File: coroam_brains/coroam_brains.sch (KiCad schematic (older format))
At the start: 19 parts, among them U1 L7805, U2 mini_esp32

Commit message: trying schematic on new pc
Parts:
- C1, C2, C3, C4, C5: symbol Device:CP -> coroam_brains-rescue:CP-Device
- D1, D2: symbol Device:LED -> coroam_brains-rescue:LED-Device
- LCD_I2C1: symbol Connector:Screw_Terminal_01x04 -> coroam_brains-rescue:Screw_Terminal_01x04-Connector
- R1, R2, oneWirePup1: symbol Device:R -> coroam_brains-rescue:R-Device
- TempBreadBoard1, TempCasing1, TempElectronics1, TempLaser1, TempWater1: symbol Connector:Screw_Terminal_01x03 -> coroam_brains-rescue:Screw_Terminal_01x03-Connector
- U1: symbol Regulator_Linear:L7805 -> coroam_brains-rescue:L7805-Regulator_Linear
- U2: symbol laserhannes_custom:mini_esp32 -> coroam_brains-rescue:mini_esp32-laserhannes_custom
- lls1: symbol laserhannes_custom:level_shifter -> coroam_brains-rescue:level_shifter-laserhannes_custom
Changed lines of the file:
@@
 EESchema Schematic File Version 4
-LIBS:coroam_brains-cache
 EELAYER 30 0
 EELAYER END
@@
 $EndDescr
 $Comp
-L power:+3.3V #PWR018
+L coroam_brains-rescue:+3.3V-power #PWR018
 U 1 1 5F539EF8
 P 6550 2900
@@
 $EndComp
 $Comp
-L power:GND #PWR017
+L coroam_brains-rescue:GND-power #PWR017
 U 1 1 5F53B2BB
 P 6450 3500
@@
 Connection ~ 6450 3400
 $Comp
-L power:+5V #PWR015
+L coroam_brains-rescue:+5V-power #PWR015
 U 1 1 5F543A46
 P 6300 2900
@@
 	6300 3000 6250 3000
 $Comp
-L power:+5V #PWR02
+L coroam_brains-rescue:+5V-power #PWR02
 U 1 1 5F540B62
 P 1200 900
@@
 $EndComp
 $Comp
-L power:GND #PWR05
+L coroam_brains-rescue:GND-power #PWR05
 U 1 1 5F540B68
 P 1800 1750
@@
 $EndComp
 $Comp
-L Regulator_Linear:L7805 U1
+L coroam_brains-rescue:L7805-Regulator_Linear U1
 U 1 1 5F540B6E
 P 3250 950
@@
 $EndComp
 $Comp
-L power:+12V #PWR09
+L coroam_brains-rescue:+12V-power #PWR09
 U 1 1 5F540B74
 P 2750 900
@@
 	2750 950  2950 950
 $Comp
-L power:GND #PWR010
+L coroam_brains-rescue:GND-power #PWR010
 U 1 1 5F540B82
 P 3250 1400
@@
 Connection ~ 2750 950
 $Comp
-L Device:CP C5
+L coroam_brains-rescue:CP-Device C5
 U 1 1 5F540B8F
 P 3650 1150
@@
 	3650 950  3550 950
 $Comp
-L power:+5V #PWR011
+L coroam_brains-rescue:+5V-power #PWR011
 U 1 1 5F540B99
 P 3650 900
@@
 12V -> 5V conversion
 $Comp
-L Device:CP C2
+L coroam_brains-rescue:CP-Device C2
 U 1 1 5F540BA6
 P 1200 1100
@@
 	1200 900  1200 950
 $Comp
-L Device:R R1
+L coroam_brains-rescue:R-Device R1
 U 1 1 5F540BAD
 P 1800 1100
@@
 $EndComp
 $Comp
-L power:+5V #PWR04
+L coroam_brains-rescue:+5V-power #PWR04
 U 1 1 5F540BB3
 P 1800 900
@@
 	1800 900  1800 950
 $Comp
-L Device:LED D1
+L coroam_brains-rescue:LED-Device D1
 U 1 1 5F540BBA
 P 1800 1400
@@
 $EndComp
 $Comp
-L Device:R R2
+L coroam_brains-rescue:R-Device R2
 U 1 1 5F540BC0
 P 2150 1100
@@
 	2150 900  2150 950
 $Comp
-L Device:LED D2
+L coroam_brains-rescue:LED-Device D2
 U 1 1 5F540BC7
 P 2150 1400
@@
 $EndComp
 $Comp
-L power:+12V #PWR06
+L coroam_brains-rescue:+12V-power #PWR06
 U 1 1 5F540BCD
 P 2150 900
@@
 $EndComp
 $Comp
-L Device:CP C3
+L coroam_brains-rescue:CP-Device C3
 U 1 1 5F540BD3
 P 1500 1100
@@
 $EndComp
 $Comp
-L power:+12V #PWR03
+L coroam_brains-rescue:+12V-power #PWR03
 U 1 1 5F540BD9
 P 1500 900
@@
 PWR LEDs + Capacitors\n\n
 $Comp
-L Device:CP C4
+L coroam_brains-rescue:CP-Device C4
 U 1 1 5F540B7C
 P 2750 1150
@@
 $EndComp
 $Comp
-L laserhannes_custom:level_shifter lls1
+L coroam_brains-rescue:level_shifter-laserhannes_custom lls1
 U 1 1 5F53B58D
 P 6350 1300
@@
 $EndComp
 $Comp
-L power:GND #PWR016
+L coroam_brains-rescue:GND-power #PWR016
 U 1 1 5F53CC9D
 P 6350 1800
@@
 Connection ~ 6350 1750
 $Comp
-L power:+5V #PWR019
+L coroam_brains-rescue:+5V-power #PWR019
 U 1 1 5F54055C
 P 6800 850
@@
 	1800 1550 1800 1700
 $Comp
-L Device:CP C1
+L coroam_brains-rescue:CP-Device C1
 U 1 1 5F54CF6A
 P 900 1100
@@
 	900  1250 900  1700
 $Comp
-L power:+3.3V #PWR01
+L coroam_brains-rescue:+3.3V-power #PWR01
 U 1 1 5F550889
 P 900 900
@@
 	750  2000 750  650
 $Comp
-L power:+3.3V #PWR014
+L coroam_brains-rescue:+3.3V-power #PWR014
 U 1 1 5F55DB2F
 P 5850 850
@@
 	5850 1250 5950 1250
 $Comp
-L Sensor_Temperature:DS18B20 #VirtTempSens1
+L coroam_brains-rescue:DS18B20-Sensor_Temperature #VirtTempSens1
 U 1 1 5F5A15DA
 P 1600 2850
@@
 	1600 3150 1850 3150
 $Comp
-L power:VCC #PWR012
+L coroam_brains-rescue:VCC-power #PWR012
 U 1 1 5F5A168D
 P 5200 900
@@
 	5200 1000 5200 900
 $Comp
-L power:GND #PWR013
+L coroam_brains-rescue:GND-power #PWR013
 U 1 1 5F5A1695
 P 5200 1350
@@
 	1850 2950 2400 2950
 $Comp
-L Connector:Screw_Terminal_01x03 TempLaser1
+L coroam_brains-rescue:Screw_Terminal_01x03-Connector TempLaser1
 U 1 1 5F5A16BA
 P 2200 2850
@@
 	5350 1650 5350 650
 $Comp
-L Device:R oneWirePup1
+L coroam_brains-rescue:R-Device oneWirePup1
 U 1 1 5F5A1745
 P 2700 2600
@@
 $EndComp
 $Comp
-L power:+3.3V #PWR07
+L coroam_brains-rescue:+3.3V-power #PWR07
 U 1 1 5F61D207
 P 2500 2450
@@
 $EndComp
 $Comp
-L Connector:Screw_Terminal_01x03 TempWater1
+L coroam_brains-rescue:Screw_Terminal_01x03-Connector TempWater1
 U 1 1 5F637CDD
 P 2200 3200
@@
 $EndComp
 $Comp
-L laserhannes_custom:mini_esp32 U2
+L coroam_brains-rescue:mini_esp32-laserhannes_custom U2
 U 1 1 5F53A6B0
 P 5700 2900
@@
 $EndComp
 $Comp
-L power:GND #PWR08
+L coroam_brains-rescue:GND-power #PWR08
 U 1 1 5F5A16C8
 P 2600 4350
@@
 Connection ~ 2500 2750
 $Comp
-L Motor:Fan_4pin #Fan1
+L coroam_brains-rescue:Fan_4pin-Motor #Fan1
 U 1 1 5F654C7A
 P 4250 3200
@@
 $EndComp
 $Comp
-L Motor:Fan_4pin #Fan2
+L coroam_brains-rescue:Fan_4pin-Motor #Fan2
 U 1 1 5F657083
 P 4250 3850
@@
 $EndComp
 $Comp
-L Motor:Fan_4pin #Fan3
+L coroam_brains-rescue:Fan_4pin-Motor #Fan3
 U 1 1 5F657A07
 P 4250 4550
@@
 $EndComp
 $Comp
-L Connector:Screw_Terminal_01x03 TempCasing1
+L coroam_brains-rescue:Screw_Terminal_01x03-Connector TempCasing1
 U 1 1 5F65A7BF
 P 2200 3550
@@
 $EndComp
 $Comp
-L Connector:Screw_Terminal_01x03 TempElectronics1
+L coroam_brains-rescue:Screw_Terminal_01x03-Connector TempElectronics1
 U 1 1 5F65AD77
 P 2200 3900
@@
 Connection ~ 2400 2950
 $Comp
-L Connector:Screw_Terminal_01x03 TempBreadBoard1
+L coroam_brains-rescue:Screw_Terminal_01x03-Connector TempBreadBoard1
 U 1 1 5F68CFDD
 P 2200 4250
@@
 DS18B20 based temperature sensing
 $Comp
-L Connector:Screw_Terminal_01x04 LCD_I2C1
+L coroam_brains-rescue:Screw_Terminal_01x04-Connector LCD_I2C1
 U 1 1 5F5A1687
 P 4800 1200

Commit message: minor brain sch changes
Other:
- note added: "Door Open/Close\n"
- note added: "LED Strips (status + case)\n"
- note added: "Laser Shutter Servo Control"
- note added: "OLED Screen"
- note added: "Pump / Fan Control"
- note added: "Pump / Fan Sensing?"
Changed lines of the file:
@@
 Connection ~ 2500 2750
 $Comp
-L coroam_brains-rescue:Fan_4pin-Motor #Fan1
+L coroam_brains-rescue:Fan_4pin-Motor #CaseFans1
 U 1 1 5F654C7A
-P 4250 3200
-F 0 "#Fan1" H 4408 3250 50  0000 L CNN
-F 1 "Fan_4pin" H 4408 3205 50  0001 L CNN
-F 2 "" H 4250 3210 50  0001 C CNN
-F 3 "http://www.formfactors.org/developer%5Cspecs%5Crev1_2_public.pdf" H 4250 3210 50  0001 C CNN
-	1    4250 3200
+P 2750 5350
+F 0 "#CaseFans1" H 2908 5400 50  0000 L CNN
+F 1 "Fan_4pin" H 2908 5355 50  0001 L CNN
+F 2 "" H 2750 5360 50  0001 C CNN
+F 3 "http://www.formfactors.org/developer%5Cspecs%5Crev1_2_public.pdf" H 2750 5360 50  0001 C CNN
+	1    2750 5350
 	1    0    0    -1
 $EndComp
 $Comp
-L coroam_brains-rescue:Fan_4pin-Motor #Fan2
+L coroam_brains-rescue:Fan_4pin-Motor #RadiatorFans1
 U 1 1 5F657083
-P 4250 3850
-F 0 "#Fan2" H 4408 3900 50  0000 L CNN
-F 1 "Fan_4pin" H 4408 3855 50  0001 L CNN
-F 2 "" H 4250 3860 50  0001 C CNN
-F 3 "http://www.formfactors.org/developer%5Cspecs%5Crev1_2_public.pdf" H 4250 3860 50  0001 C CNN
-	1    4250 3850
+P 1900 5350
+F 0 "#RadiatorFans1" H 2058 5400 50  0000 L CNN
+F 1 "Fan_4pin" H 2058 5355 50  0001 L CNN
+F 2 "" H 1900 5360 50  0001 C CNN
+F 3 "http://www.formfactors.org/developer%5Cspecs%5Crev1_2_public.pdf" H 1900 5360 50  0001 C CNN
+	1    1900 5350
 	1    0    0    -1
 $EndComp
 $Comp
-L coroam_brains-rescue:Fan_4pin-Motor #Fan3
+L coroam_brains-rescue:Fan_4pin-Motor #Pump1
 U 1 1 5F657A07
-P 4250 4550
-F 0 "#Fan3" H 4408 4600 50  0000 L CNN
-F 1 "Fan_4pin" H 4408 4555 50  0001 L CNN
-F 2 "" H 4250 4560 50  0001 C CNN
-F 3 "http://www.formfactors.org/developer%5Cspecs%5Crev1_2_public.pdf" H 4250 4560 50  0001 C CNN
-	1    4250 4550
+P 1100 5350
+F 0 "#Pump1" H 1258 5400 50  0000 L CNN
+F 1 "Fan_4pin" H 1258 5355 50  0001 L CNN
+F 2 "" H 1100 5360 50  0001 C CNN
+F 3 "http://www.formfactors.org/developer%5Cspecs%5Crev1_2_public.pdf" H 1100 5360 50  0001 C CNN
+	1    1100 5350
 	1    0    0    -1
 $EndComp
@@
 DS18B20 based temperature sensing
 Text Notes 4100 650  0    50   ~ 0
-DS18B20 based temperature sensing
+OLED Screen
 $Comp
 L coroam_brains-rescue:Screw_Terminal_01x04-Connector LCD_I2C1
@@
 	-1   0    0    1
 $EndComp
+Text Notes 850  5000 0    50   ~ 0
+Pump / Fan Control
+Text Notes 850  5800 0    50   ~ 0
+Pump / Fan Sensing?
+Text Notes 850  6250 0    50   ~ 0
+LED Strips (status + case)\n
+Text Notes 850  6700 0    50   ~ 0
+Door Open/Close\n
+Text Notes 2750 6250 0    50   ~ 0
+Laser Shutter Servo Control
 $EndSCHEMATC

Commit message: finishing brains schematics
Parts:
- added C10, C?: 100u, Capacitor_THT:CP_Radial_D6.3mm_P2.50mm, symbol coroam_brains-rescue:CP-Device
- added C6, C7, C8: 22u, Capacitor_THT:CP_Radial_D5.0mm_P2.50mm, symbol coroam_brains-rescue:CP-Device
- added C9: 10u, Capacitor_THT:CP_Radial_D5.0mm_P2.50mm, symbol coroam_brains-rescue:CP-Device
- added CaseFan1, Pump1, RadiatorFan1: Fan_4pin, Connector:FanPinHeader_1x04_P2.54mm_Vertical, symbol coroam_brains-rescue:Fan_4pin-Motor
- added D3, D4, D5: D_Small_ALT, Diode_SMD:D_SMB_Handsoldering, symbol Device:D_Small_ALT
- added J1: OpenCirc, Connector_PinSocket_2.54mm:PinSocket_1x03_P2.54mm_Vertical, symbol Connector:Conn_01x03_Female
- added J2: 12V_in, TerminalBlock_Phoenix:TerminalBlock_Phoenix_PT-1,5-2-5.0-H_1x02_P5.00mm_Horizontal, symbol Connector:Screw_Terminal_01x02
- added LEDs1, LEDs?, Servo1: DigiTempSens1, Connector:FanPinHeader_1x03_P2.54mm_Vertical, symbol coroam_brains-rescue:Screw_Terminal_01x03-Connector
- added LasILock: DigiTempSens1, Connector_PinHeader_2.54mm:PinHeader_1x02_P2.54mm_Vertical, symbol Connector_Generic:Conn_01x02
- added R10, R11, R4, R9: 5.1k, Resistor_SMD:R_2010_5025Metric_Pad1.52x2.65mm_HandSolder, symbol coroam_brains-rescue:R-Device
- added R12, R13, R14, R5, R?: 10k, Resistor_SMD:R_2010_5025Metric_Pad1.52x2.65mm_HandSolder, symbol coroam_brains-rescue:R-Device
- added R15, R?: 300, Resistor_THT:R_Axial_DIN0207_L6.3mm_D2.5mm_P7.62mm_Horizontal, symbol coroam_brains-rescue:R-Device
- added RF_OA, RF_PD: ~, Connector_Coaxial:SMB_Jack_Vertical, symbol Connector_Generic:Conn_01x02
- added lls?: level_shifter, laserhannes_custom:level_shifte, symbol coroam_brains-rescue:level_shifter-laserhannes_custom
- C1, C2, C3: value 4.7u -> 22u
- C4: footprint Capacitor_THT:CP_Radial_D5.0mm_P2.50mm -> Capacitor_SMD:C_1206_3216Metric_Pad1.42x1.75mm_HandSolder
- C5: footprint Capacitor_THT:CP_Radial_D5.0mm_P2.50mm -> Capacitor_SMD:C_0603_1608Metric_Pad1.05x0.95mm_HandSolder
- D1: value Red -> 5V
- D2: value Green -> 12V
- R1: value 150 -> 300; footprint Resistor_THT:R_Axial_DIN0414_L11.9mm_D4.5mm_P15.24mm_Horizontal -> Resistor_THT:R_Axial_DIN0207_L6.3mm_D2.5mm_P7.62mm_Horizontal
- R2: value 560 -> 1k; footprint Resistor_THT:R_Axial_DIN0414_L11.9mm_D4.5mm_P15.24mm_Horizontal -> Resistor_THT:R_Axial_DIN0207_L6.3mm_D2.5mm_P7.62mm_Horizontal
- renumbered oneWirePup1 to R?
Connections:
- net VCC is gone; now on net +3V3: LCD_I2C1.4 (Pin_4)
- net +12V: now also C10.1, C6.1, C7.1, C8.1, C?.1, CaseFan1.2 (+), D3.1 (K), D4.1 (K), D5.1 (K), J2.1 (Pin_1), LEDs1.3 (Pin_3), LEDs?.3 (Pin_3), Pump1.2 (+), RadiatorFan1.2 (+)
- net +3V3: now also R?.1, lls?.3 (LV_IN)
- net +5V: now also C9.1, J1.3 (Pin_3), Servo1.2 (Pin_2), lls?.10 (HV_IN)
- net GND: now also C10.2, C6.2, C7.2, C8.2, C9.2, C?.2, CaseFan1.1 (-), D3.2 (A), D4.2 (A), D5.2 (A), J1.1 (Pin_1), J1.2 (Pin_2), J2.2 (Pin_2), LEDs1.1 (Pin_1), LEDs?.1 (Pin_1), LasILock.1 (Pin_1), Pump1.1 (-), R12.1, R13.1, R14.1, R4.2, R5.1, RF_OA.2 (Pin_2), RF_PD.2 (Pin_2), RadiatorFan1.1 (-), Servo1.1 (Pin_1), lls?.4 (GND), lls?.9 (GND)
- net RadFanPWM_3V: now reaches U2.10 (IO_19/D6)
- net RadFanPWM_3V: now also lls1.6 (LV4)
- net LED_CTRL: now reaches U2.11 (IO_34)
- net Servo_3V: now reaches U2.24 (IO_27)
- net Servo_3V: now also lls1.1 (LV1)
- net Door_3V: now reaches U2.26 (IO_25)
- net Door_3V: now also R4.1, R5.2
- net Interlock: now reaches U2.28 (IO_32)
- net Interlock: now also LasILock.2 (Pin_2), R?.2
- net STATUS_LED_3V: now reaches U2.30 (IO_12/TDI)
- net STATUS_LED_3V: now also lls?.2 (LV2)
- net CASE_LED_3V: now reaches U2.32 (IO_04)
- net CASE_LED_3V: now also lls?.1 (LV1)
- net RF_SWITCH_3V: now reaches U2.34 (IO_00)
- net PumpTach_3V: now reaches U2.5 (IO_39/SVN)
- net PumpTach_3V: now also R11.1, R14.2
- net PumpPWM_3V: now reaches U2.6 (IO_26/D0)
- net PumpPWM_3V: now also lls1.2 (LV2)
- net CaseFanTach_3V: now reaches U2.7 (IO_35)
- net CaseFanTach_3V: now also R10.1, R13.2
- net CaseFanPWM_3V: now reaches U2.8 (IO_18/D5)
- net CaseFanPWM_3V: now also lls1.5 (LV3)
- net RadFanTach_3V: now reaches U2.9 (IO_33)
- net RadFanTach_3V: now also R12.2, R9.1
- net PumpPWM: now reaches lls1.11 (HV2)
- net PumpPWM: now also Pump1.4 (PWM)
- net Servo_5V: now reaches lls1.12 (HV1)
- net Servo_5V: now also Servo1.3 (Pin_3)
- net RadFanPWM: now reaches lls1.7 (HV4)
- net RadFanPWM: now also RadiatorFan1.4 (PWM)
- net CaseFanPWM: now reaches lls1.8 (HV3)
- net CaseFanPWM: now also CaseFan1.4 (PWM)
- new net: LEDs?.2 (Pin_2), R?.2
- new net: LEDs1.2 (Pin_2), R15.2
- new net CASE_LED_5V: R?.1, lls?.12 (HV1)
- new net CaseFanTach: CaseFan1.3 (Tacho), R10.2
- new net PumpTach: Pump1.3 (Tacho), R11.2
- new net RF_SW_OA_3V: RF_OA.1 (Pin_1)
- new net RF_SW_PD_3V: RF_PD.1 (Pin_1)
- new net RadFanTach: R9.2, RadiatorFan1.3 (Tacho)
- new net STATUS_LED_5V: R15.1, lls?.11 (HV2)
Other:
- note added: "5V <-> 3.3V level shifting"
- note added: "Laser Interlock Ctrl"
- note added: "Need to figure out\nhow many LEDS I need...\n"
- note added: "Pump + fan control and sensing"
- note added: "RF Switch Control"
- note removed: "Pump / Fan Control"
- note removed: "Pump / Fan Sensing?"
- moved on the sheet: U2, lls1

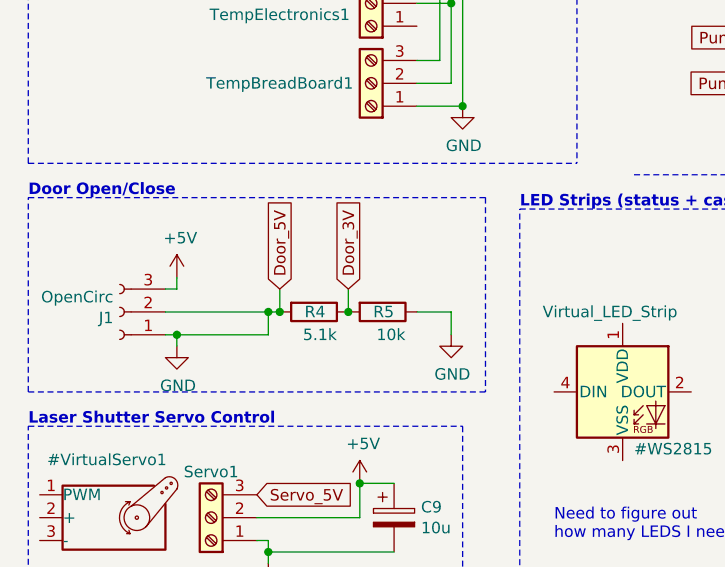
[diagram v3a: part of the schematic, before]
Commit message: minor bug fix on coroam brain
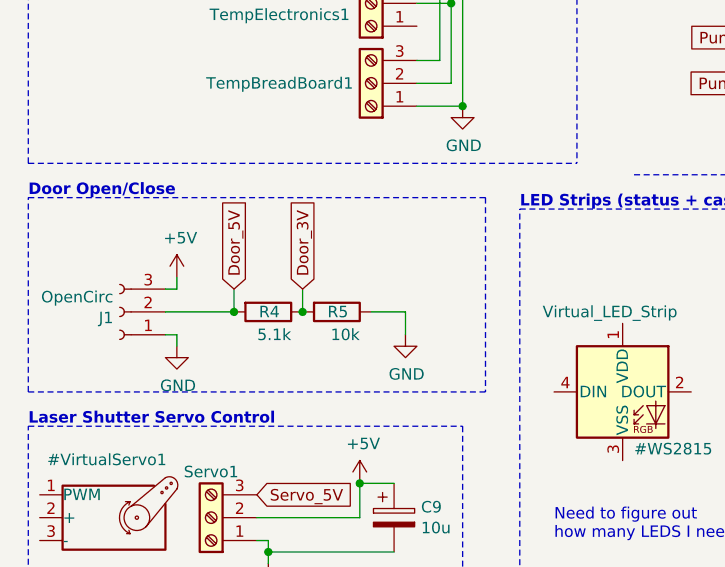
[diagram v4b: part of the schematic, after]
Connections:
- net GND: no longer J1.2 (Pin_2), R4.2
- new net Door_5V: J1.2 (Pin_2), R4.2
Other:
- moved on the sheet: R4, R5
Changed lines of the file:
@@
 Wire Wire Line
 	1350 5150 1350 5100
-Connection ~ 1350 5350
-Wire Wire Line
-	1750 5350 1750 5250
-Wire Wire Line
-	1300 5250 1750 5250
-Wire Wire Line
-	1800 5250 1750 5250
-Connection ~ 1750 5250
 Text GLabel 6150 1200 0    50   Input ~ 0
 PumpPWM_3V
@@
 Text GLabel 6150 1600 0    50   Input ~ 0
 RadFanPWM_3V
-Text GLabel 2100 5150 1    50   Input ~ 0
-Door_3V
-Text GLabel 1800 5150 1    50   Input ~ 0
-Door_5V
-$Comp
-L coroam_brains-rescue:R-Device R5
-U 1 1 5F76259E
-P 2250 5250
-F 0 "R5" V 2250 5300 50  0000 R CNN
-F 1 "10k" V 2350 5350 50  0000 R CNN
-F 2 "Resistor_SMD:R_2010_5025Metric_Pad1.52x2.65mm_HandSolder" V 2180 5250 50  0001 C CNN
-F 3 "http://industrial.panasonic.com/cdbs/www-data/pdf/RDA0000/AOA0000C301.pdf" H 2250 5250 50  0001 C CNN
-	1    2250 5250
-	0    1    1    0
-$EndComp
-$Comp
-L coroam_brains-rescue:R-Device R4
-U 1 1 5F763355
-P 1950 5250
-F 0 "R4" V 1950 5300 50  0000 R CNN
-F 1 "5.1k" V 2050 5350 50  0000 R CNN
-F 2 "Resistor_SMD:R_2010_5025Metric_Pad1.52x2.65mm_HandSolder" V 1880 5250 50  0001 C CNN
-F 3 "https://industrial.panasonic.com/cdbs/www-data/pdf/RDA0000/AOA0000C304.pdf" H 1950 5250 50  0001 C CNN
-	1    1950 5250
-	0    1    1    0
-$EndComp
-$Comp
-L coroam_brains-rescue:GND-power #PWR022
-U 1 1 5F7650B8
-P 2550 5350
-F 0 "#PWR022" H 2550 5100 50  0001 C CNN
-F 1 "GND" H 2555 5177 50  0000 C CNN
-F 2 "" H 2550 5350 50  0001 C CNN
-F 3 "" H 2550 5350 50  0001 C CNN
-	1    2550 5350
-	1    0    0    -1
-$EndComp
-Wire Wire Line
-	2550 5250 2550 5350
-Wire Wire Line
-	2400 5250 2550 5250
-Wire Wire Line
-	2100 5150 2100 5250
-Connection ~ 2100 5250
-Wire Wire Line
-	1800 5150 1800 5250
-Connection ~ 1800 5250
 $Comp
 L coroam_brains-rescue:R-Device R9
@@
 Wire Wire Line
 	6050 900  6050 1300
-Wire Wire Line
-	1350 5350 1750 5350
 $Comp
 L coroam_brains-rescue:Fan_4pin-Motor CaseFan1
@@
 	1    0    0    -1
 $EndComp
+Wire Wire Line
+	1600 5150 1600 5250
+Connection ~ 1900 5250
+Wire Wire Line
+	1900 5150 1900 5250
+Wire Wire Line
+	2200 5250 2350 5250
+Wire Wire Line
+	2350 5250 2350 5350
+$Comp
+L coroam_brains-rescue:GND-power #PWR022
+U 1 1 5F7650B8
+P 2350 5350
+F 0 "#PWR022" H 2350 5100 50  0001 C CNN
+F 1 "GND" H 2355 5177 50  0000 C CNN
+F 2 "" H 2350 5350 50  0001 C CNN
+F 3 "" H 2350 5350 50  0001 C CNN
+	1    2350 5350
+	1    0    0    -1
+$EndComp
+$Comp
+L coroam_brains-rescue:R-Device R4
+U 1 1 5F763355
+P 1750 5250
+F 0 "R4" V 1750 5300 50  0000 R CNN
+F 1 "5.1k" V 1850 5350 50  0000 R CNN
+F 2 "Resistor_SMD:R_2010_5025Metric_Pad1.52x2.65mm_HandSolder" V 1680 5250 50  0001 C CNN
+F 3 "https://industrial.panasonic.com/cdbs/www-data/pdf/RDA0000/AOA0000C304.pdf" H 1750 5250 50  0001 C CNN
+	1    1750 5250
+	0    1    1    0
+$EndComp
+$Comp
+L coroam_brains-rescue:R-Device R5
+U 1 1 5F76259E
+P 2050 5250
+F 0 "R5" V 2050 5300 50  0000 R CNN
+F 1 "10k" V 2150 5350 50  0000 R CNN
+F 2 "Resistor_SMD:R_2010_5025Metric_Pad1.52x2.65mm_HandSolder" V 1980 5250 50  0001 C CNN
+F 3 "http://industrial.panasonic.com/cdbs/www-data/pdf/RDA0000/AOA0000C301.pdf" H 2050 5250 50  0001 C CNN
+	1    2050 5250
+	0    1    1    0
+$EndComp
+Text GLabel 1600 5150 1    50   Input ~ 0
+Door_5V
+Text GLabel 1900 5150 1    50   Input ~ 0
+Door_3V
+Wire Wire Line
+	1300 5250 1600 5250
+Connection ~ 1600 5250
 $EndSCHEMATC

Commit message: fixing few more bugs
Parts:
- added C12: 10u, Capacitor_THT:CP_Radial_D5.0mm_P2.50mm, symbol coroam_brains-rescue:CP-Device
- added D6: D_Small_ALT, Diode_SMD:D_SMB_Handsoldering, symbol Device:D_Small_ALT
- added J3: RF_pwr, TerminalBlock_Phoenix:TerminalBlock_Phoenix_PT-1,5-2-5.0-H_1x02_P5.00mm_Horizontal, symbol Connector:Screw_Terminal_01x02
- added R7, R8: 10k, Resistor_SMD:R_2010_5025Metric_Pad1.52x2.65mm_HandSolder, symbol coroam_brains-rescue:R-Device
- C6, C7, C8: value 22u -> 10u
- gave numbers to parts that had none: 6
- renumbered LasILock to LasILock1, RF_OA to RF_OA1, RF_PD to RF_PD1
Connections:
- net RF_SW_OA_3V is gone; now on net RF_SW_OA: RF_OA1.1 (Pin_1)
- net RF_SW_PD_3V is gone; now on net RF_SW_PD: RF_PD1.1 (Pin_1)
- net +5V: now also C12.1, D6.1 (K), J3.2 (Pin_2)
- net GND: now also C12.2, D6.2 (A), J3.1 (Pin_1), R7.1, R8.1
- net STATUS_LED_3V: now also U2.13 (IO_14/TMS); no longer U2.30 (IO_12/TDI)
- net RF_SW_OA: now reaches U2.14 (IO_05/D8)
- net RF_SW_OA: now also R7.2
- net LED_CTRL renamed RF_SW_PD
- net RF_SW_PD: now also R8.2
- net RF_SWITCH_3V: no longer names the net of U2.34 (IO_00)
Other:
- note added: "FIX FAN TACH READ PULLUP!\n"
- moved on the sheet: C10, C11, C9, J1, LEDs1, LEDs2, R15, R4, R5, R6, RF_OA1, RF_PD1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
